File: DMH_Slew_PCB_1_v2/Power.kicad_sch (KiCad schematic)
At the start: 11 parts, among them J0 Conn_01x01, J101 IDC_02x08, U7 LM4040LP-10

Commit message: Notes while breadboarding
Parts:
- added C10, C11: 100nF, Capacitor_THT:C_Disc_D4.3mm_W1.9mm_P5.00mm, symbol Device:C
- added U1: TL072, symbol Amplifier_Operational:TL072
- added U2: TL074, symbol Amplifier_Operational:TL074
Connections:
- net +12V: now also C10.1, U1.8 (V+), U2.4 (V+)
- net -12V: now also C11.2, U1.4 (V-), U2.11 (V-)
- net GND: now also C10.2, C11.1

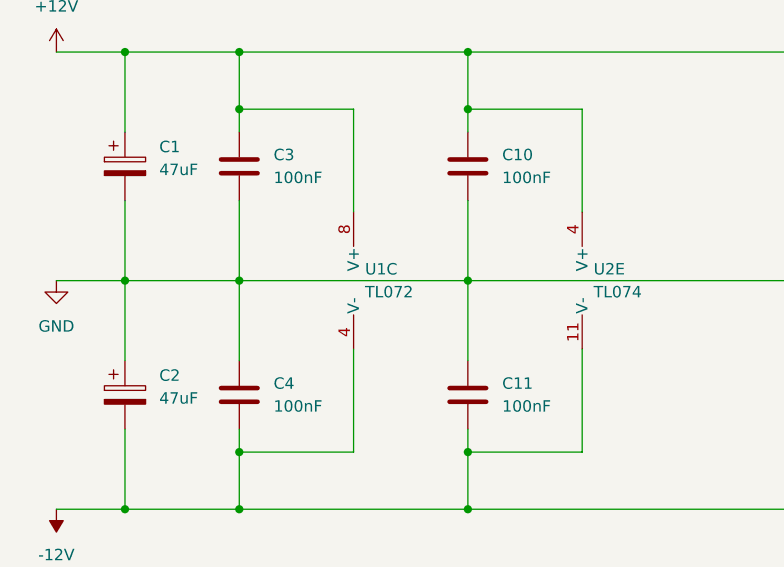
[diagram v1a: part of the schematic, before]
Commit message: Added state gate outputs circuit
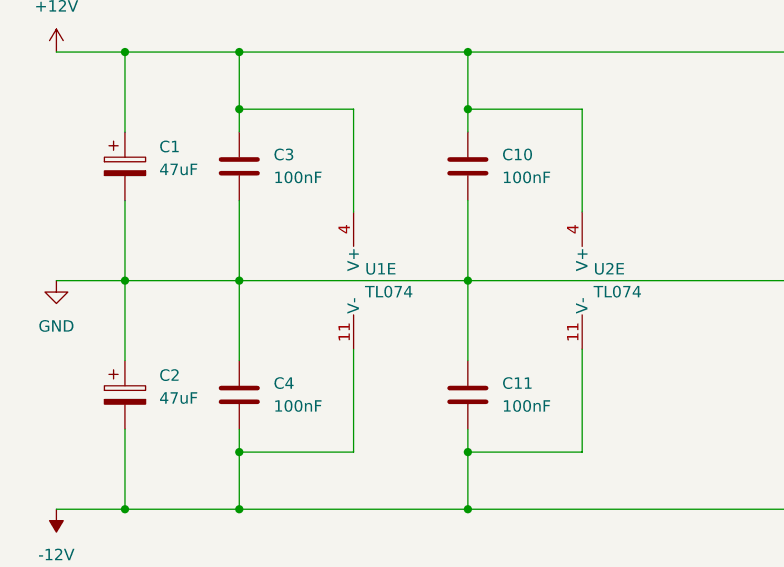
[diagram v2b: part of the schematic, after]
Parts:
- removed U1: TL072, symbol Amplifier_Operational:TL072
- added U1: TL074, Package_DIP:DIP-16_W7.62mm_Socket, symbol Amplifier_Operational:TL074
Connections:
- net +12V: now also U1.4 (V+)
- net -12V: now also U1.11 (V-)
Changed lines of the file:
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@@
+	)
+	(symbol
+		(lib_id "Amplifier_Operational:TL074")
+		(at 53.34 120.65 0)
+		(unit 5)
+		(exclude_from_sim no)
+		(in_bom yes)
+		(on_board yes)
+		(dnp no)
+		(fields_autoplaced yes)
+		(property "Reference" "U1"
+			(at 52.07 119.3799 0)
+			(effects
+				(font
+					(size 1.27 1.27)
+				)
+				(justify left)
+			)
+		)
+		(property "Value" "TL074"
+			(at 52.07 121.9199 0)
+			(effects
+				(font
+					(size 1.27 1.27)
+				)
+				(justify left)
+			)
+		)
+		(property "Footprint" "Package_DIP:DIP-16_W7.62mm_Socket"
+			(at 52.07 118.11 0)
+			(effects
+				(font
+					(size 1.27 1.27)
+				)
+				(hide yes)
+			)
+		)
+		(property "Datasheet" "http://www.ti.com/lit/ds/symlink/tl071.pdf"
+			(at 54.61 115.57 0)
+			(effects
+				(font
+					(size 1.27 1.27)
+				)
+				(hide yes)
+			)
+		)
+		(property "Description" "Quad Low-Noise JFET-Input Operational Amplifiers, DIP-14/SOIC-14"
+			(at 53.34 120.65 0)
+			(effects
+				(font
+					(size 1.27 1.27)
+				)
+				(hide yes)
+			)
+		)
+		(property "Function" ""
+			(at 53.34 120.65 0)
+			(effects
+				(font
+					(size 1.27 1.27)
+				)
+			)
+		)
+		(pin "6"
+		)
+		(pin "4"
+		)
+		(pin "2"
+		)
+		(pin "10"
+		)
+		(pin "14"
+		)
+		(pin "11"
+		)
+		(pin "9"
+		)
+		(pin "3"
+		)
+		(pin "1"
+		)
+		(pin "7"
+		)
+		(pin "5"
+		)
+		(pin "8"
+		)
+		(pin "12"
+		)
+		(pin "13"
+		)
+		(instances
+			(project ""
+				(path "/58f4306d-5387-4983-bb08-41a2313fd315/0cdf34b2-39cd-4d9e-981a-97cd34791509"
+					(reference "U1")
+					(unit 5)
+				)
+			)
+		)
 	)
 	(symbol
@@
 				)
 			)
-		)
-	)
-	(symbol
-		(lib_id "Amplifier_Operational:TL072")
-		(at 53.34 120.65 0)
-		(unit 3)
-		(exclude_from_sim no)
-		(in_bom yes)
-		(on_board yes)
-		(dnp no)
-		(fields_autoplaced yes)
-		(property "Reference" "U1"
-			(at 52.07 119.3799 0)
-			(effects
-				(font
-					(size 1.27 1.27)
-				)
-				(justify left)
-			)
-		)
-		(property "Value" "TL072"
-			(at 52.07 121.9199 0)
-			(effects
-				(font
-					(size 1.27 1.27)
-				)
-				(justify left)
-			)
-		)
-		(property "Footprint" ""
-			(at 53.34 120.65 0)
-			(effects
-				(font
-					(size 1.27 1.27)
-				)
-				(hide yes)
-			)
-		)
-		(property "Datasheet" "http://www.ti.com/lit/ds/symlink/tl071.pdf"
-			(at 53.34 120.65 0)
-			(effects
-				(font
-					(size 1.27 1.27)
-				)
-				(hide yes)
-			)
-		)
-		(property "Description" "Dual Low-Noise JFET-Input Operational Amplifiers, DIP-8/SOIC-8"
-			(at 53.34 120.65 0)
-			(effects
-				(font
-					(size 1.27 1.27)
-				)
-				(hide yes)
-			)
-		)
-		(pin "1"
-		)
-		(pin "6"
-		)
-		(pin "7"
-		)
-		(pin "5"
-		)
-		(pin "4"
-		)
-		(pin "8"
-		)
-		(pin "3"
-		)
-		(pin "2"
-		)
-		(instances
-			(project ""
-				(path "/58f4306d-5387-4983-bb08-41a2313fd315/0cdf34b2-39cd-4d9e-981a-97cd34791509"
-					(reference "U1")
-					(unit 3)
-				)
-			)

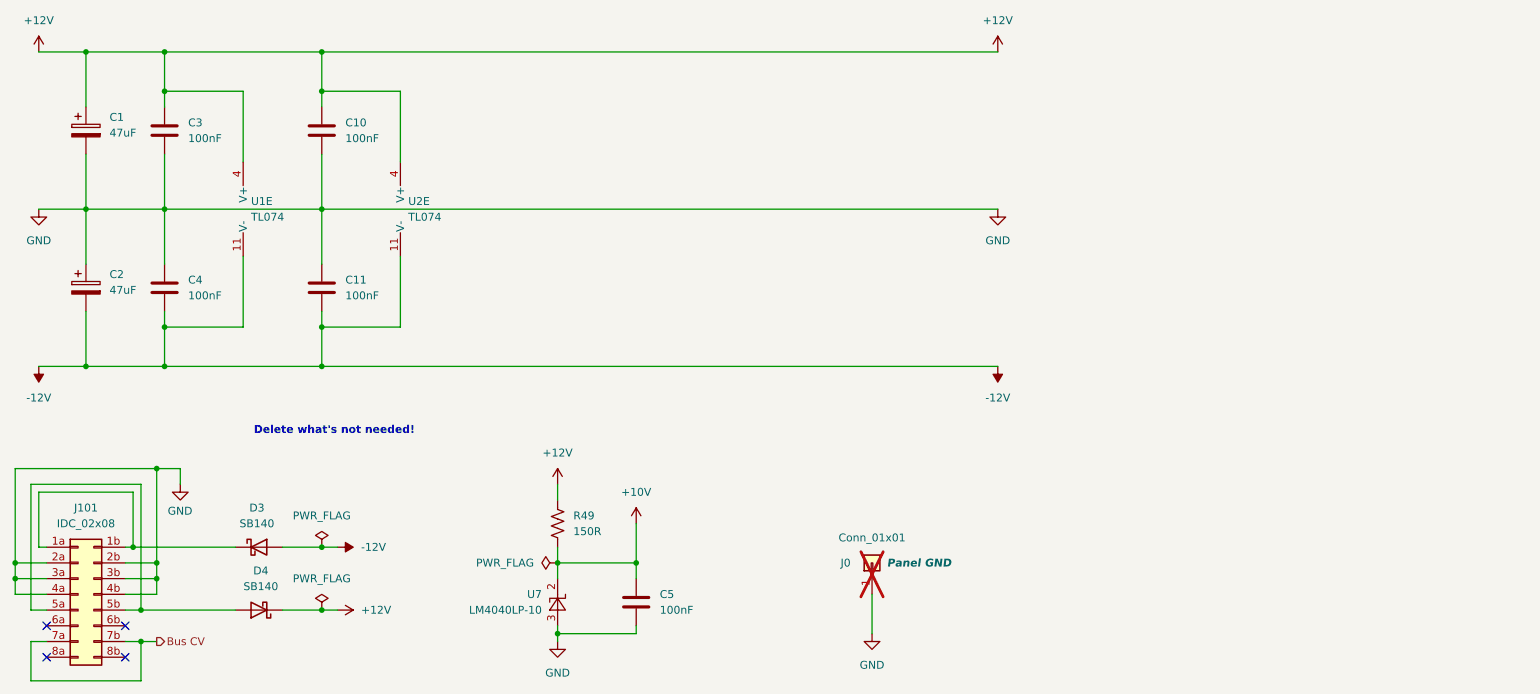
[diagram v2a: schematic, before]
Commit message: Separating PCB 1 and 2 in schematic
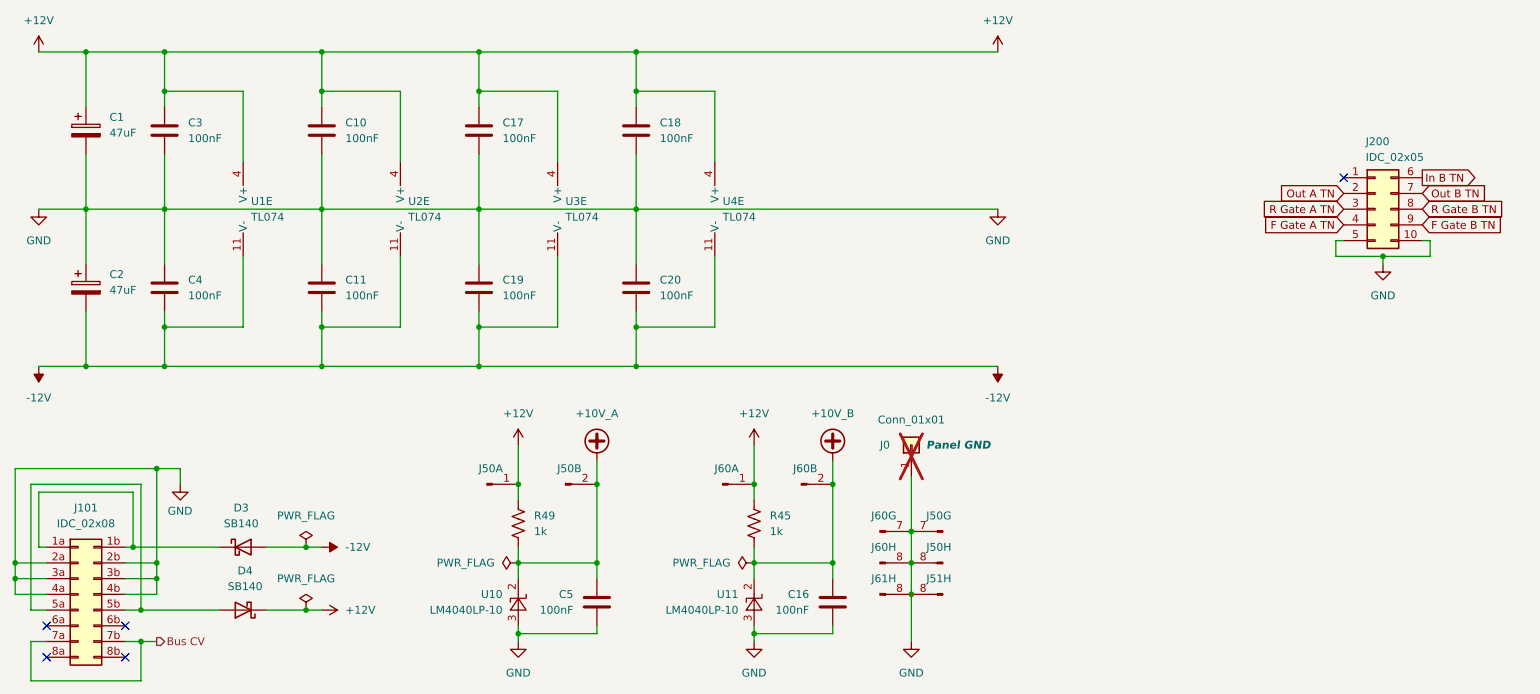
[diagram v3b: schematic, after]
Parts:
- added C16, C17, C18, C19, C20: 100nF, Capacitor_THT:C_Disc_D4.3mm_W1.9mm_P5.00mm, symbol Device:C
- added J200: IDC_02x05, SynthStuff:IDC-Header_2x05_P2.54mm_Vertical_BackBone, symbol SynthStuff:BackBone_Connector_10Pin
- added J50, J51, J60, J61: Conn_01x08_PinHeader, Connector_PinHeader_2.54mm:PinHeader_1x08_P2.54mm_Vertical, symbol SynthStuff:Conn_01x08_PinHeader
- added R45: 1k, Resistor_THT:R_Axial_DIN0207_L6.3mm_D2.5mm_P7.62mm_Horizontal, symbol Device:R_US
- added U11: LM4040LP-10, Package_TO_SOT_THT:TO-92_Inline, symbol Reference_Voltage:LM4040LP-10
- added U3: TL074, Package_DIP:DIP-16_W7.62mm_Socket, symbol Amplifier_Operational:TL074
- added U4: TL074, Package_DIP:DIP-14_W7.62mm_Socket, symbol Amplifier_Operational:TL074
- R49: value 150R -> 1k
- U2: footprint (none) -> Package_DIP:DIP-14_W7.62mm_Socket
- renumbered U7 to U10
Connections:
- net +12V: now also C17.1, C18.1, J50.1 (Pin_1), J60.1 (Pin_1), R45.2, U3.4 (V+), U4.4 (V+)
- net -12V: now also C19.2, C20.2, U3.11 (V-), U4.11 (V-)
- net GND: now also C16.2, C17.2, C18.2, C19.1, C20.1, J200.10 (Pin_10), J200.5 (Pin_5), J50.7 (Pin_7), J50.8 (Pin_8), J51.8 (Pin_8), J60.7 (Pin_7), J60.8 (Pin_8), J61.8 (Pin_8), U11.3 (A)
- net +10V renamed +10V_A
- net +10V_A: now also J50.2 (Pin_2)
- new net +10V_B: C16.1, J60.2 (Pin_2), R45.1, U11.2 (K)
- new net F Gate A TN: J200.4 (Pin_4)
- new net F Gate B TN: J200.9 (Pin_9)
- new net In B TN: J200.6 (Pin_6)
- new net Out A TN: J200.2 (Pin_2)
- new net Out B TN: J200.7 (Pin_7)
- new net R Gate A TN: J200.3 (Pin_3)
- new net R Gate B TN: J200.8 (Pin_8)
- no-connect marks 4 -> 5
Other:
- note removed: "Delete what's not needed!"
- moved on the sheet: C5, D3, D4, J0, R49, U10
